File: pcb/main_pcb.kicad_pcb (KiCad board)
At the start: 2 copper layers, 62 x 67 mm, 34 parts, among them J1 Conn_01x06_Socket, J2 Conn_01x10_Pin, J3 Conn_01x06_Pin, J4 USB_C_Receptacle_USB2.0, Q1 Si2323DS, SW1 SW_Push, SW2 SW_Push, SW3 SW_Push, U1 ESP32-H2-MINI-1, U2 LM5165Y

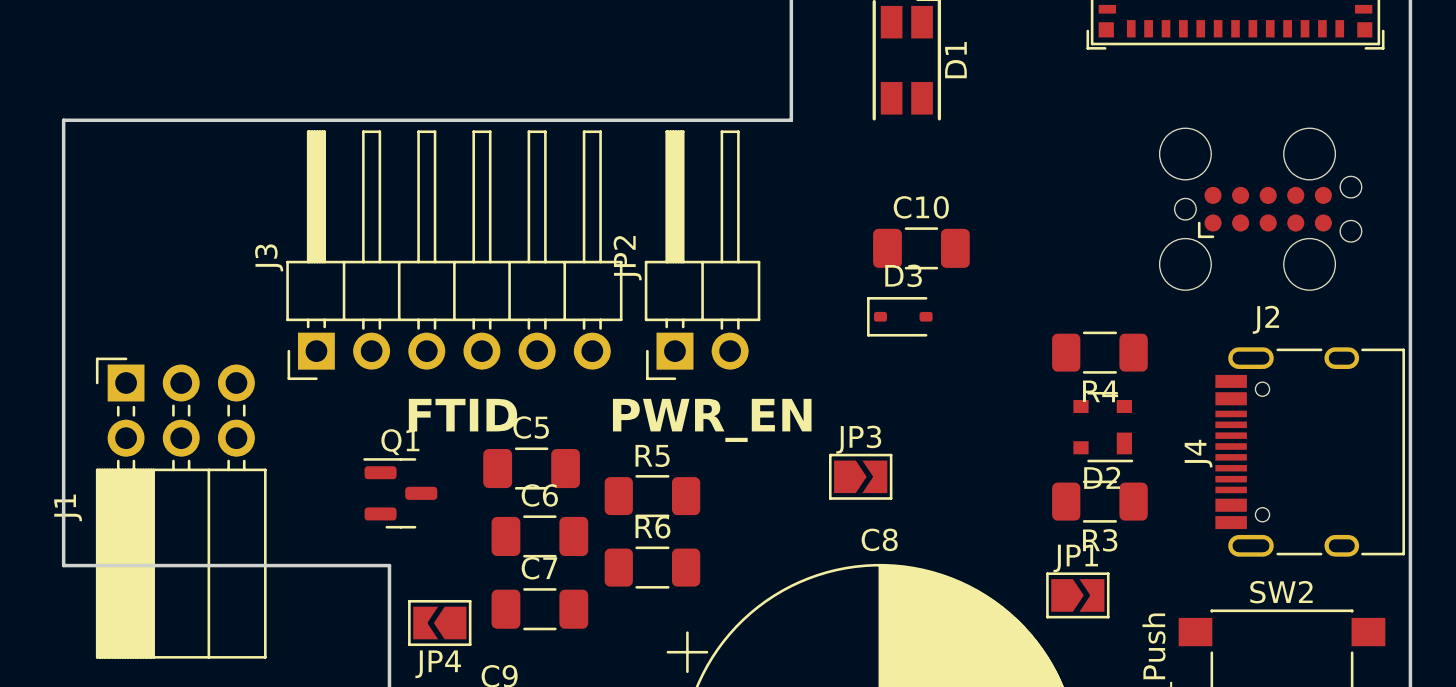
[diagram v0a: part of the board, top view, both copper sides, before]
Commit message: Replace FTDI power pin jumper with solder bridge
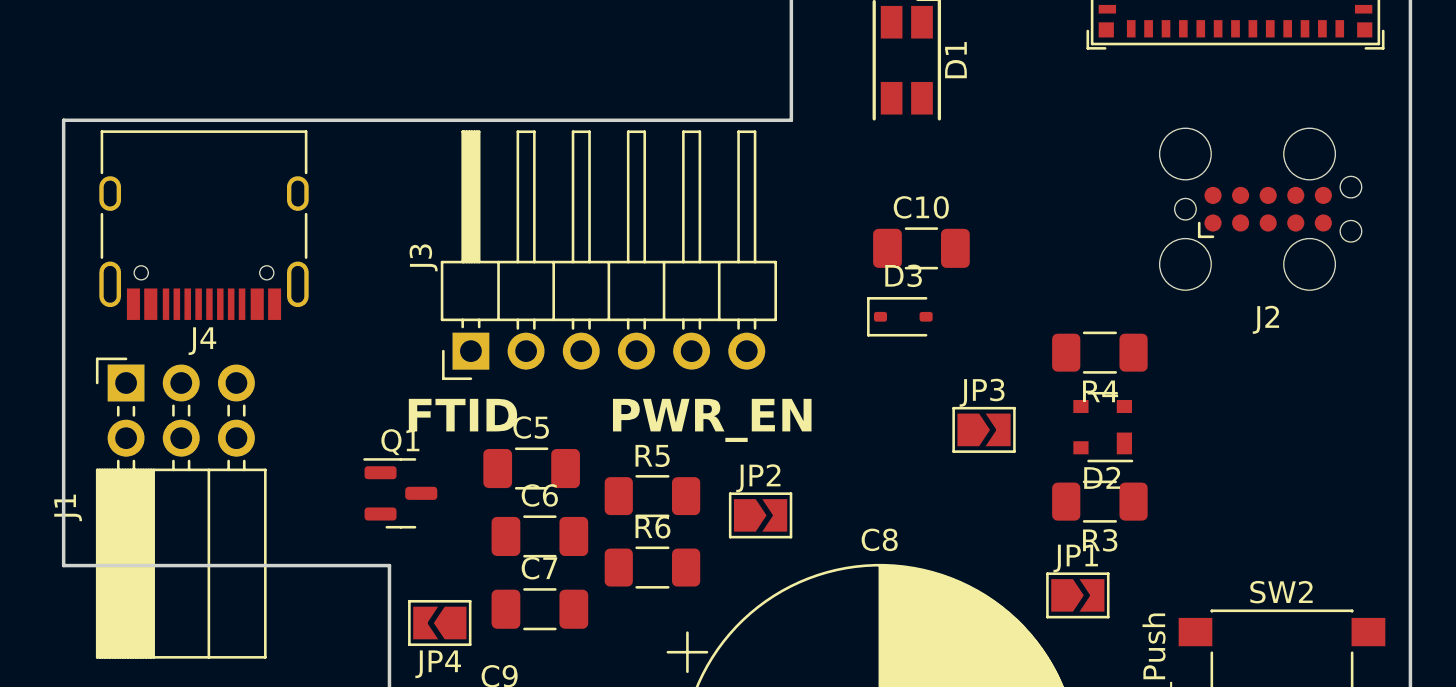
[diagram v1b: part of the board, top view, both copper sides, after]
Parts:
- JP2: value Jumper_2_Open -> SolderJumper_2_Bridged; footprint Connector_PinHeader_2.54mm:PinHeader_1x02_P2.54mm_Horizontal -> Jumper:SolderJumper-2_P1.3mm_Open_TrianglePad1.0x1.5mm
- moved J4 52.5 mm to (115.5, 68.7), turned to 180 degrees
- moved JP2 8.53 mm to (141.1, 82.4), turned to 0 degrees
- moved J3 7.11 mm to (127.8, 74.9)
- moved JP3 6.07 mm to (151.4, 78.5)

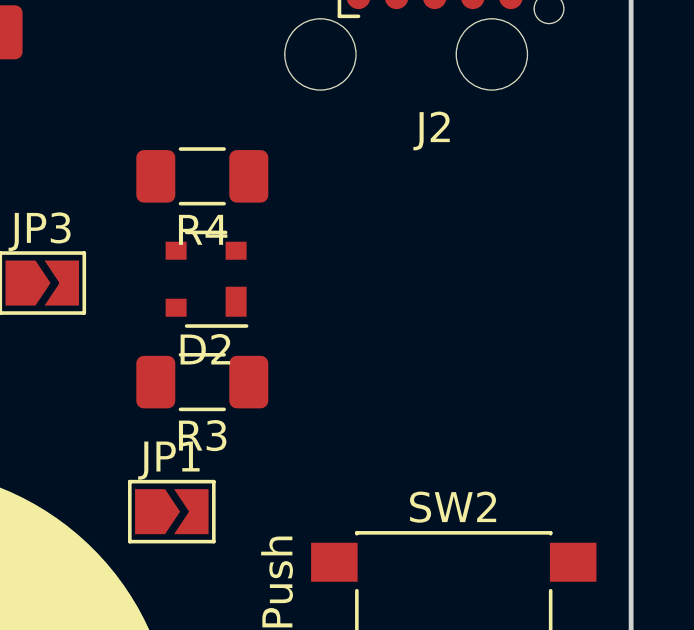
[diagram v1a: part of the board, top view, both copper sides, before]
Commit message: Add pair button circuit
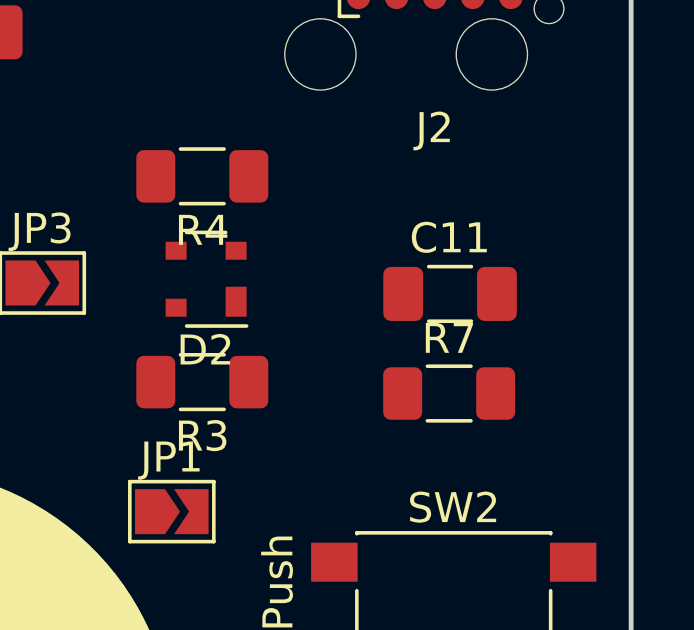
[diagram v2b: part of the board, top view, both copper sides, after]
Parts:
- added C11: 1uF, Capacitor_SMD:C_1206_3216Metric_Pad1.33x1.80mm_HandSolder, F.Cu at (165.0, 78.8)
- added R7: 10k, Resistor_SMD:R_1206_3216Metric_Pad1.30x1.75mm_HandSolder, F.Cu at (164.9, 82.2)
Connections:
- SW1 pad 1: unconnected-(SW1-Pad1) -> /PAIR
- SW1 pad 2: unconnected-(SW1-Pad2) -> +3.3V
- U1 pad 24: unconnected-(U1-GPIO22-Pad24) -> /PAIR

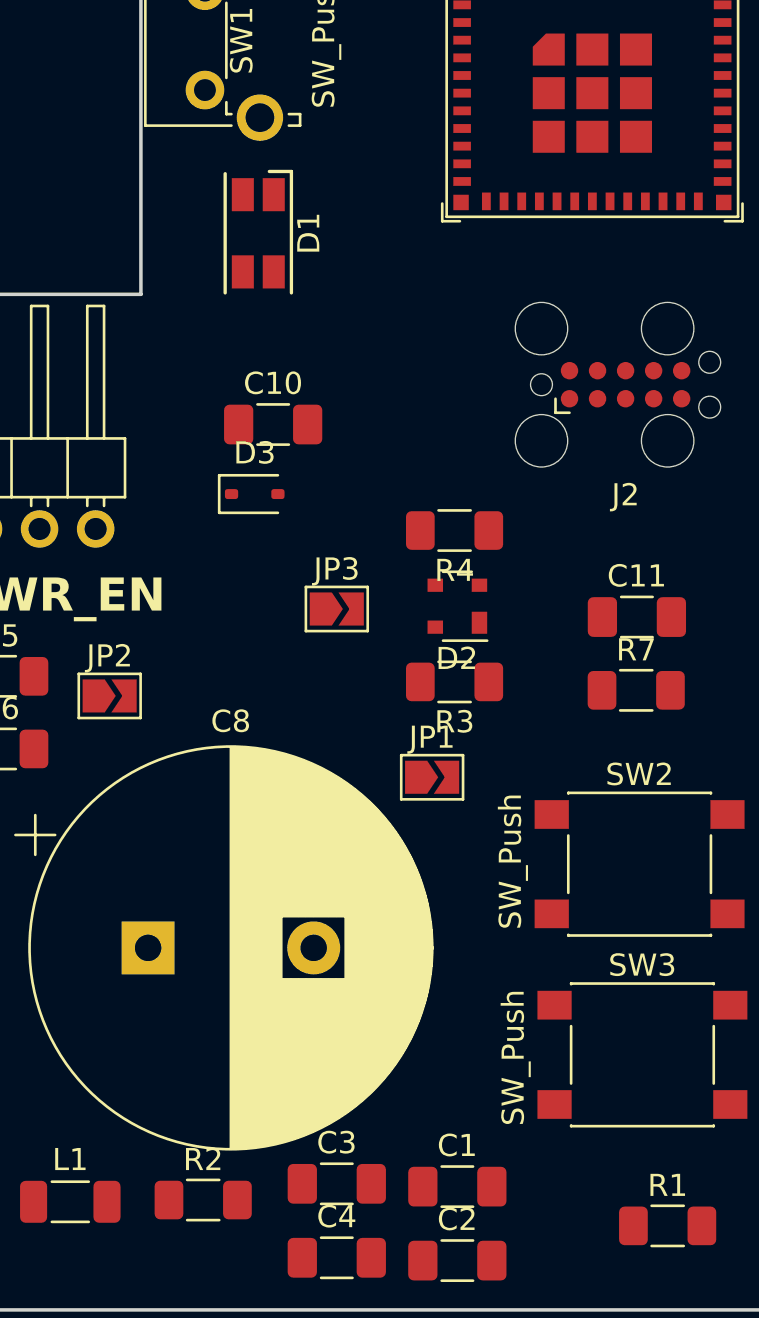
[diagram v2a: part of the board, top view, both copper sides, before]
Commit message: Add status LED circuit
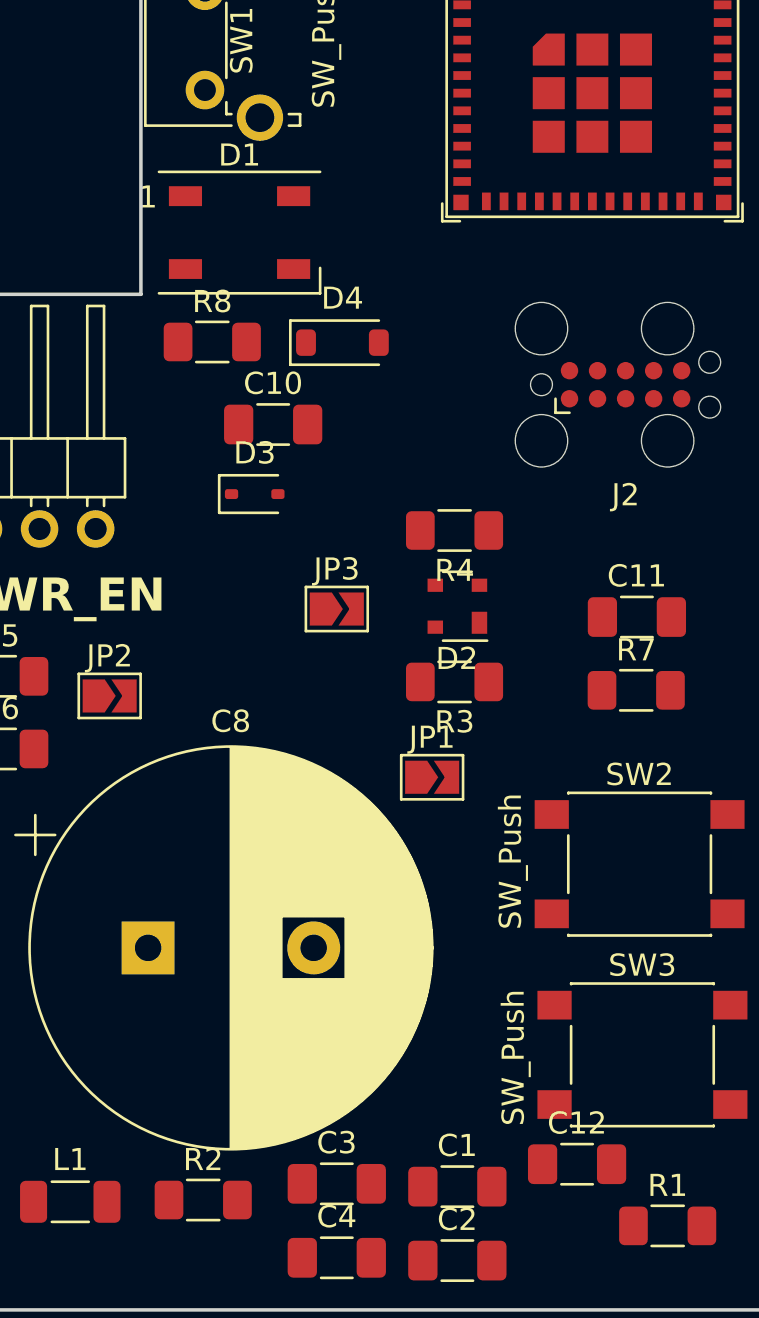
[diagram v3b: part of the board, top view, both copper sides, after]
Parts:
- added C12: 0.1uF, Capacitor_SMD:C_1206_3216Metric_Pad1.33x1.80mm_HandSolder, F.Cu at (162.3, 103.6)
- added D4: 1N4148W, Diode_SMD:D_SOD-123, F.Cu at (151.6, 66.4)
- added R8: 10k, Resistor_SMD:R_1206_3216Metric_Pad1.30x1.75mm_HandSolder, F.Cu at (145.7, 66.4)
- D1: value LED_RAGB -> WS2812B; footprint LED_SMD:LED_RGB_1210 -> LED_SMD:LED_WS2812B_PLCC4_5.0x5.0mm_P3.2mm
- moved D1 0.85 mm to (147.0, 61.4), turned to 0 degrees
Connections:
- D1 pad 1: unconnected-(D1-RK-Pad1) -> VDD
- D1 pad 3: unconnected-(D1-GK-Pad3) -> GND
- D1 pad 4: unconnected-(D1-BK-Pad4) -> Net-(D1-DIN)
- U1 pad 25: unconnected-(U1-GPIO25/FSPICS3-Pad25) -> /LED

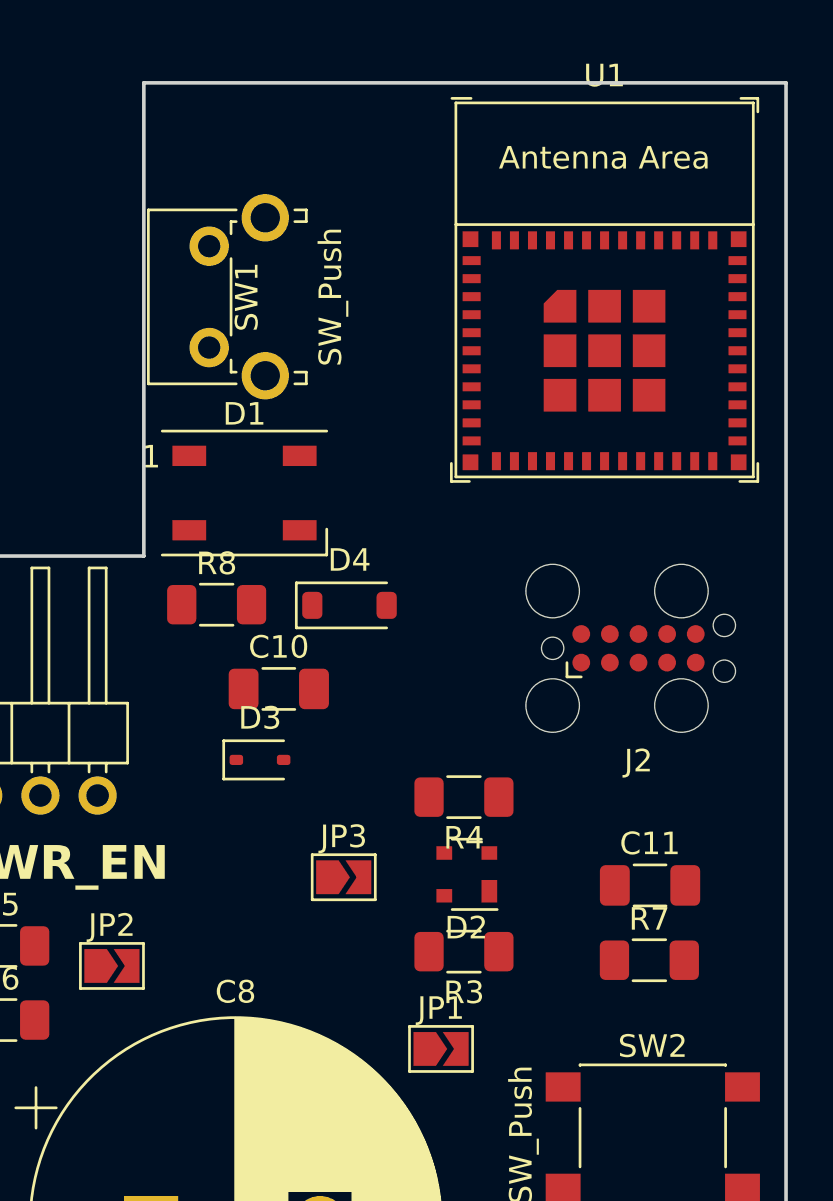
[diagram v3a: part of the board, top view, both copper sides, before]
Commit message: Add RTC crystal circuit
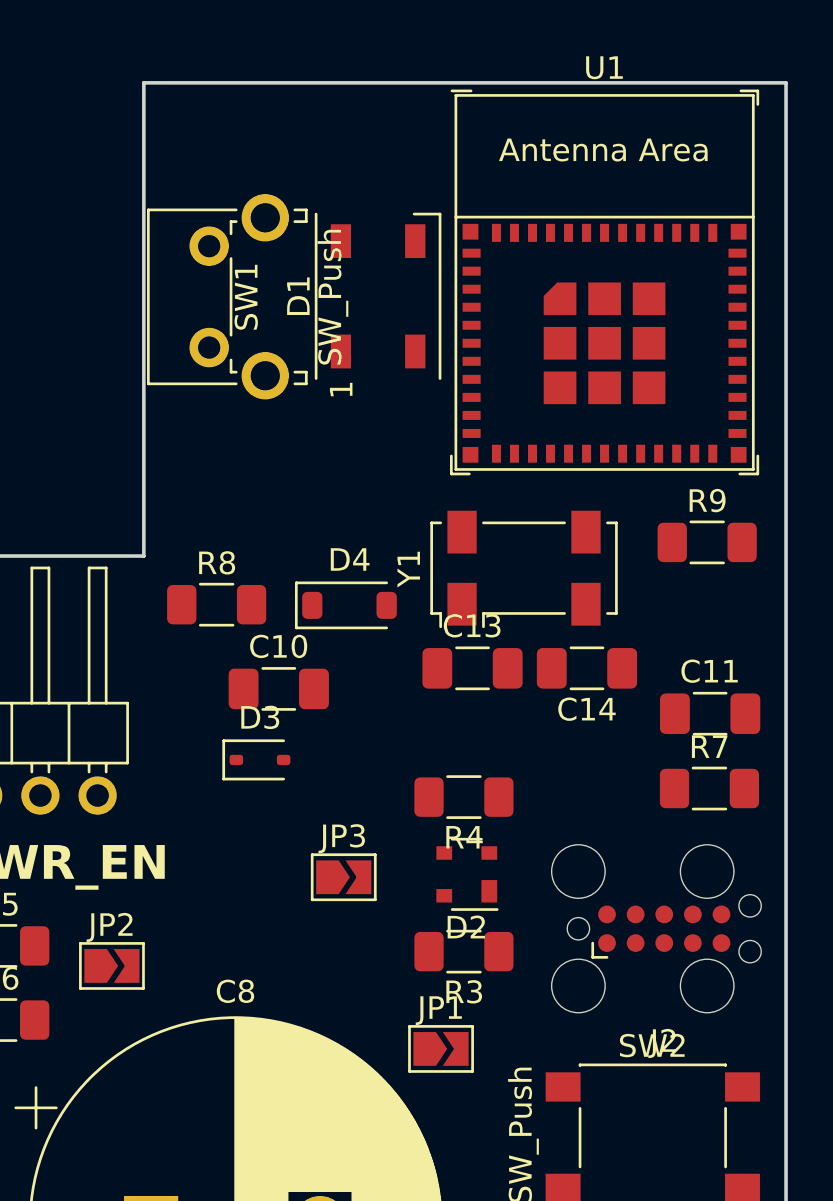
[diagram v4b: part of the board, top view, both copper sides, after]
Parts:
- added C13: 12pF, Capacitor_SMD:C_1206_3216Metric_Pad1.33x1.80mm_HandSolder, F.Cu at (157.1, 69.2)
- added C14: 12pF, Capacitor_SMD:C_1206_3216Metric_Pad1.33x1.80mm_HandSolder, F.Cu at (162.2, 69.2)
- added R9: 5.1M, Resistor_SMD:R_1206_3216Metric_Pad1.30x1.75mm_HandSolder, F.Cu at (167.5, 63.6)
- added Y1: 32.768KHz, Crystal:Crystal_SMD_Abracon_ABS25-4Pin_8.0x3.8mm, F.Cu at (159.4, 64.8)
- moved J2 12.5 mm to (165.6, 80.8)
- moved D1 10.6 mm to (152.9, 52.7), turned to 90 degrees
- moved C11 8.07 mm to (167.6, 71.2)
- moved R7 8.07 mm to (167.6, 74.5)
- moved U1 0.33 mm to (163.0, 52.1)
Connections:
- U1 pad 12: unconnected-(U1-GPIO13/XTAL_32K_P-Pad12) -> Net-(U1-GPIO13/XTAL_32K_P)
- U1 pad 13: unconnected-(U1-GPIO14/XTAL_32K_N-Pad13) -> Net-(U1-GPIO14/XTAL_32K_N)

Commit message: Remove FTDI connector
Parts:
- removed J3: Conn_01x06_Pin, Connector_PinHeader_2.54mm:PinHeader_1x06_P2.54mm_Horizontal
- removed JP2: SolderJumper_2_Bridged, Jumper:SolderJumper-2_P1.3mm_Open_TrianglePad1.0x1.5mm
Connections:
- C10 pad 2: unconnected-(C10-Pad2) -> GND
- U1 pad 1: Net-(U1-GND-Pad1) -> GND
- U1 pad 11: Net-(U1-GND-Pad1) -> GND
- U1 pad 14: Net-(U1-GND-Pad1) -> GND
- U1 pad 2: Net-(U1-GND-Pad1) -> GND
- U1 pad 36: Net-(U1-GND-Pad1) -> GND
- U1 pad 37: Net-(U1-GND-Pad1) -> GND
- U1 pad 38: Net-(U1-GND-Pad1) -> GND
- U1 pad 39: Net-(U1-GND-Pad1) -> GND
- U1 pad 40: Net-(U1-GND-Pad1) -> GND
- U1 pad 41: Net-(U1-GND-Pad1) -> GND
- U1 pad 42: Net-(U1-GND-Pad1) -> GND
- U1 pad 43: Net-(U1-GND-Pad1) -> GND
- U1 pad 44: Net-(U1-GND-Pad1) -> GND
- U1 pad 45: Net-(U1-GND-Pad1) -> GND
- U1 pad 46: Net-(U1-GND-Pad1) -> GND
- U1 pad 47: Net-(U1-GND-Pad1) -> GND
- U1 pad 48: Net-(U1-GND-Pad1) -> GND
- U1 pad 49: Net-(U1-GND-Pad1) -> GND
- U1 pad 50: Net-(U1-GND-Pad1) -> GND
- U1 pad 51: Net-(U1-GND-Pad1) -> GND
- U1 pad 52: Net-(U1-GND-Pad1) -> GND
- U1 pad 53: Net-(U1-GND-Pad1) -> GND
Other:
- board text removed: "FTID"
- board text removed: "PWR_EN"

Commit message: Add HAN interface connections to ESP32
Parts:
- added R10: 0, Resistor_SMD:R_1206_3216Metric_Pad1.30x1.75mm_HandSolder, F.Cu at (134.8, 68.7)
- added R11: 0, Resistor_SMD:R_1206_3216Metric_Pad1.30x1.75mm_HandSolder, F.Cu at (134.8, 72.0)
- added R12: 0, Resistor_SMD:R_1206_3216Metric_Pad1.30x1.75mm_HandSolder, F.Cu at (134.8, 75.3)
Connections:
- J1 pad 2: /DATA_IN -> Net-(J1-Pin_2)
- J1 pad 5: /DATA_OUT -> Net-(J1-Pin_5)
- U1 pad 16: unconnected-(U1-GPIO12-Pad16) -> /DATA_IN
